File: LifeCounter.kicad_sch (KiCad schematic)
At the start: 0 parts

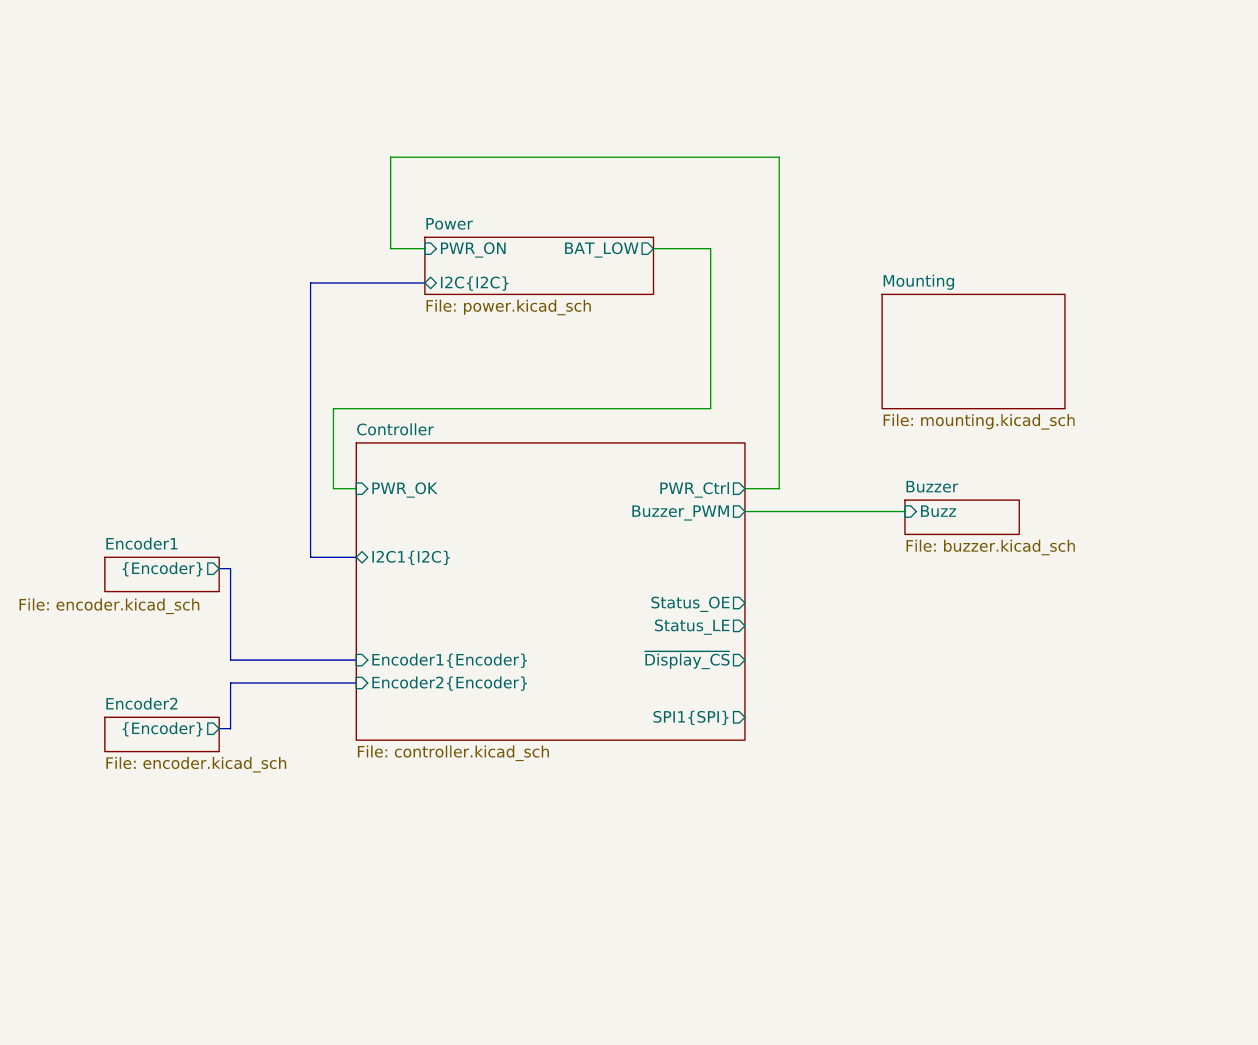
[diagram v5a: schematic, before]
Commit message: Connect displays to controller
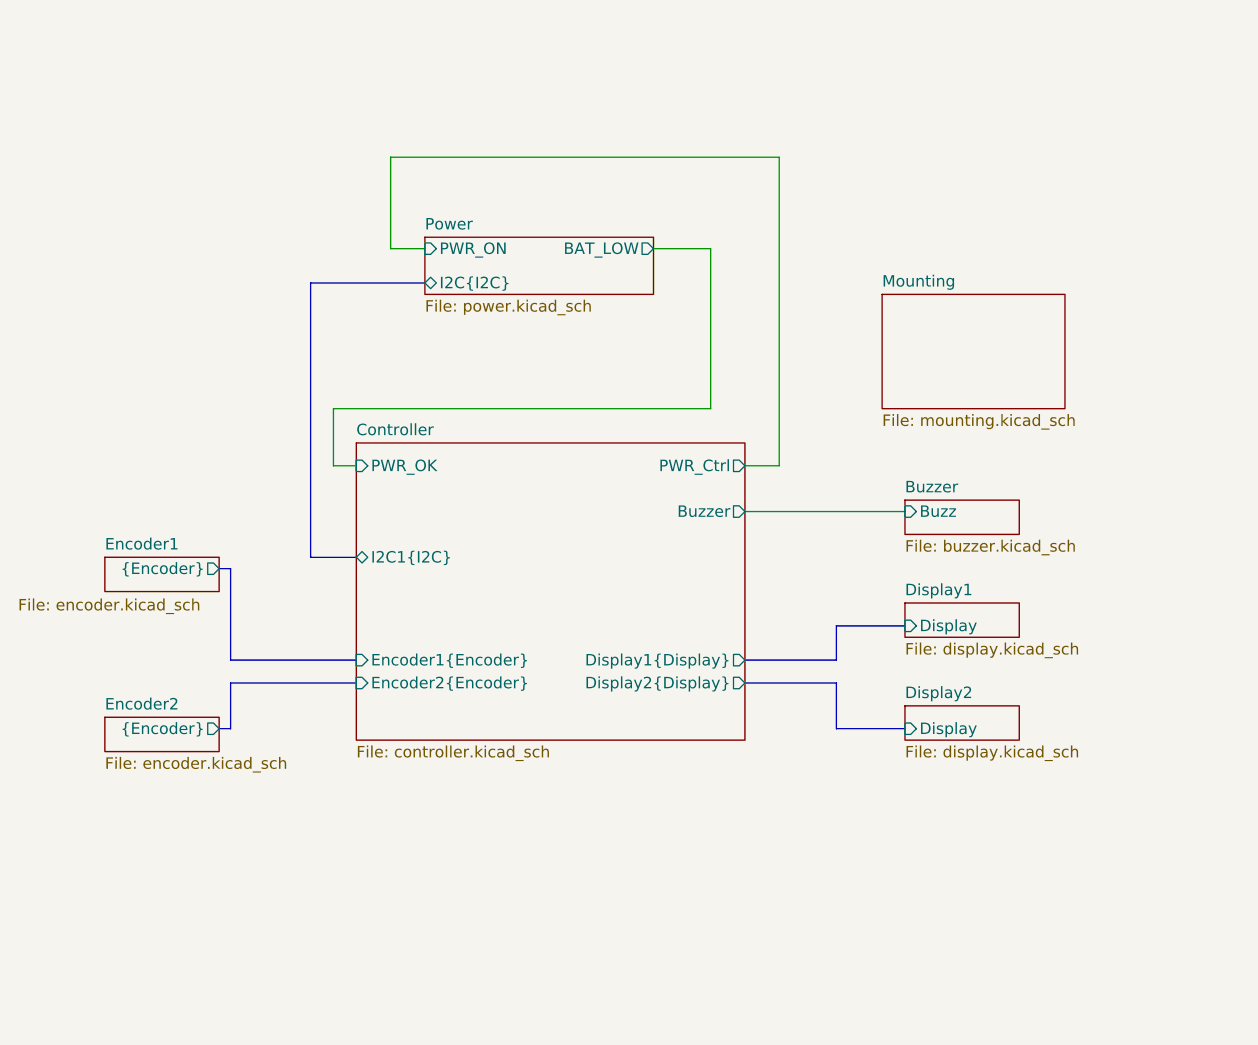
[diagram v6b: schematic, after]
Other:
- added sheet Display1 (display.kicad_sch)
- added sheet Display2 (display.kicad_sch)
- sheet Controller ports: added Buzzer, Display1{Display}, Display2{Display}; removed Buzzer_PWM, SPI1{SPI}, Status_LE, Status_OE, ~{Display_CS}
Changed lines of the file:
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@@
 	(generator_version "9.0")
 	(paper "A4")
-	(bus_alias "SEG"
-		(members "A" "B" "C" "D" "E" "F" "G" "DP")
-	)
 	(bus_alias "SPI"
 		(members "CLK" "Data")
@@
 	(wire
 		(pts
-			(xy 124.46 93.98) (xy 124.46 102.87)
+			(xy 124.46 93.98) (xy 124.46 100.33)
+		)
+		(stroke
+			(width 0)
+			(type default)
+		)
+	)
+	(bus
+		(pts
+			(xy 180.34 124.46) (xy 180.34 129.54)
 		)
 		(stroke
@@
 	(wire
 		(pts
+			(xy 124.46 100.33) (xy 127 100.33)
+		)
+		(stroke
+			(width 0)
+			(type default)
+		)
+	)
+	(wire
+		(pts
 			(xy 166.37 93.98) (xy 124.46 93.98)
 		)
@@
 	(bus
 		(pts
+			(xy 180.34 129.54) (xy 187.96 129.54)
+		)
+		(stroke
+			(width 0)
+			(type default)
+		)
+	)
+	(bus
+		(pts
 			(xy 121.92 110.49) (xy 127 110.49)
 		)
@@
 		)
 	)
-	(wire
-		(pts
-			(xy 124.46 102.87) (xy 127 102.87)
+	(bus
+		(pts
+			(xy 180.34 118.11) (xy 180.34 121.92)
 		)
 		(stroke
@@
 	(bus
 		(pts
+			(xy 187.96 118.11) (xy 180.34 118.11)
+		)
+		(stroke
+			(width 0)
+			(type default)
+		)
+	)
+	(bus
+		(pts
 			(xy 121.92 80.01) (xy 121.92 110.49)
 		)
@@
 	(wire
 		(pts
-			(xy 173.99 66.04) (xy 173.99 102.87)
-		)
-		(stroke
-			(width 0)
-			(type default)
-		)
-	)
-	(wire
-		(pts
-			(xy 173.99 102.87) (xy 170.18 102.87)
+			(xy 173.99 66.04) (xy 173.99 100.33)
+		)
+		(stroke
+			(width 0)
+			(type default)
+		)
+	)
+	(bus
+		(pts
+			(xy 170.18 124.46) (xy 180.34 124.46)
+		)
+		(stroke
+			(width 0)
+			(type default)
+		)
+	)
+	(wire
+		(pts
+			(xy 173.99 100.33) (xy 170.18 100.33)
 		)
 		(stroke
@@
 		(pts
 			(xy 166.37 76.2) (xy 166.37 93.98)
+		)
+		(stroke
+			(width 0)
+			(type default)
+		)
+	)
+	(bus
+		(pts
+			(xy 180.34 121.92) (xy 170.18 121.92)
 		)
 		(stroke
@@
 			)
 		)
-		(pin "PWR_OK" input
-			(at 127 102.87 180)
+		(pin "Buzzer" output
+			(at 170.18 105.41 0)
+			(effects
+				(font
+					(size 1.27 1.27)
+				)
+				(justify right)
+			)
+		)
+		(pin "Display1{Display}" output
+			(at 170.18 121.92 0)
+			(effects
+				(font
+					(size 1.27 1.27)
+				)
+				(justify right)
+			)
+		)
+		(pin "Display2{Display}" output
+			(at 170.18 124.46 0)
+			(effects
+				(font
+					(size 1.27 1.27)
+				)
+				(justify right)
+			)
+		)
+		(pin "Encoder1{Encoder}" input
+			(at 127 121.92 180)
+			(effects
+				(font
+					(size 1.27 1.27)
+				)
+				(justify left)
+			)
+		)
+		(pin "Encoder2{Encoder}" input
+			(at 127 124.46 180)
 			(effects
 				(font
@@
 		)
 		(pin "PWR_Ctrl" output
-			(at 170.18 102.87 0)
+			(at 170.18 100.33 0)
 			(effects
 				(font
@@
 			)
 		)
-		(pin "Encoder1{Encoder}" input
-			(at 127 121.92 180)
-			(effects
-				(font
-					(size 1.27 1.27)
-				)
-				(justify left)
-			)
-		)
-		(pin "Buzzer_PWM" output
-			(at 170.18 105.41 0)
-			(effects
-				(font
-					(size 1.27 1.27)
-				)
-				(justify right)
-			)
-		)
-		(pin "Status_OE" output
-			(at 170.18 115.57 0)
-			(effects
-				(font
-					(size 1.27 1.27)
-				)
-				(justify right)
-			)
-		)
-		(pin "Status_LE" output
-			(at 170.18 118.11 0)
-			(effects
-				(font
-					(size 1.27 1.27)
-				)
-				(justify right)
-			)
-		)
-		(pin "~{Display_CS}" output
-			(at 170.18 121.92 0)
-			(effects
-				(font
-					(size 1.27 1.27)
-				)
-				(justify right)
-			)
-		)
-		(pin "SPI1{SPI}" output
-			(at 170.18 128.27 0)
-			(effects
-				(font
-					(size 1.27 1.27)
-				)
-				(justify right)
-			)
-		)
-		(pin "Encoder2{Encoder}" input
-			(at 127 124.46 180)
+		(pin "PWR_OK" input
+			(at 127 100.33 180)
 			(effects
 				(font
@@
 	)
 	(sheet
+		(at 187.96 127)
+		(size 12.7 3.81)
+		(exclude_from_sim no)
+		(in_bom yes)
+		(on_board yes)
+		(dnp no)
+		(fields_autoplaced yes)
+		(stroke
+			(width 0.1524)
+			(type solid)
+		)
+		(fill
+			(color 0 0 0 0.0000)
+		)
+		(property "Sheetname" "Display2"
+			(at 187.96 126.2884 0)
+			(effects
+				(font
+					(size 1.27 1.27)
+				)
+				(justify left bottom)
+			)
+		)
+		(property "Sheetfile" "display.kicad_sch"
+			(at 187.96 131.3946 0)
+			(effects
+				(font
+					(size 1.27 1.27)
+				)
+				(justify left top)
+			)
+		)
+		(pin "Display" input
+			(at 187.96 129.54 180)
+			(effects
+				(font
+					(size 1.27 1.27)
+				)
+				(justify left)
+			)
+		)
+		(instances
+			(project "LifeCounter"
+				(path "/16b3e55a-9d75-49bf-a6fe-25414eb3d7da"
+					(page "3")
+				)
+			)
+		)
+	)
+	(sheet
 		(at 134.62 74.93)
 		(size 25.4 6.35)
@@
 				)
 			)
+		)
+	)
+	(sheet
+		(at 187.96 115.57)
+		(size 12.7 3.81)
+		(exclude_from_sim no)
+		(in_bom yes)
+		(on_board yes)
+		(dnp no)
+		(fields_autoplaced yes)
+		(stroke
+			(width 0.1524)
+			(type solid)
+		)
+		(fill
+			(color 0 0 0 0.0000)
+		)
+		(property "Sheetname" "Display1"
+			(at 187.96 114.8584 0)
+			(effects
+				(font
+					(size 1.27 1.27)
+				)
+				(justify left bottom)
+			)
+		)
+		(property "Sheetfile" "display.kicad_sch"
+			(at 187.96 119.9646 0)
+			(effects
+				(font
+					(size 1.27 1.27)
+				)
+				(justify left top)
+			)
+		)
+		(pin "Display" input
+			(at 187.96 118.11 180)
+			(effects
+				(font
+					(size 1.27 1.27)
+				)
+				(justify left)
+			)
+		)
+		(instances
+			(project "LifeCounter"
+				(path "/16b3e55a-9d75-49bf-a6fe-25414eb3d7da"
+					(page "8")
+				)
+			)
